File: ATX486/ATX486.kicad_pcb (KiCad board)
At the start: 2 copper layers, 1 part

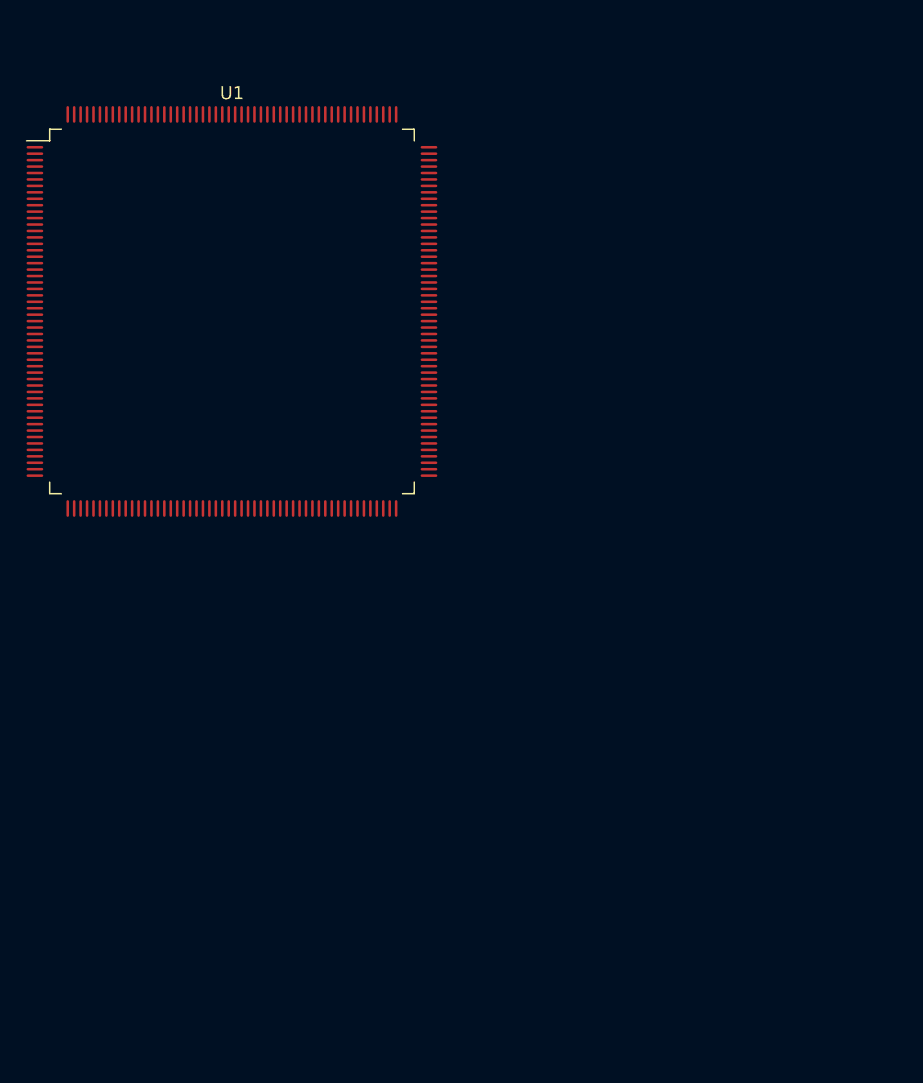
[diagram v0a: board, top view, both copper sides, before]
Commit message: Added initial southbridge info
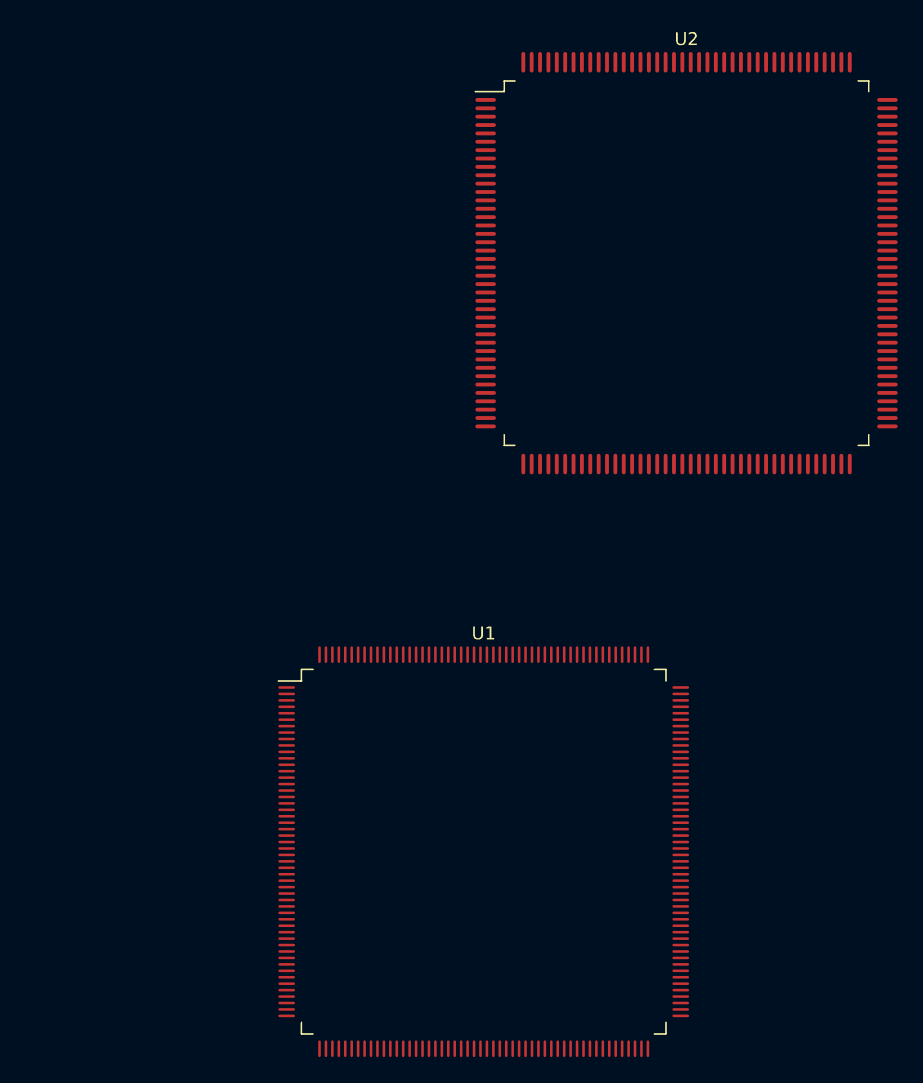
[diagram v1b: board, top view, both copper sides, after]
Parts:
- added U2: ~, Library:85C497, F.Cu at (129.5, 90.5)
- moved U1 46.3 mm to (113.8, 136.2)
